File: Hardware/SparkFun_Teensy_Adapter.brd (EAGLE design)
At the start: 7 parts, among them J1 ARDUINO_R3_SHIELD, J2 AVR_SPI_PRG_6PTH

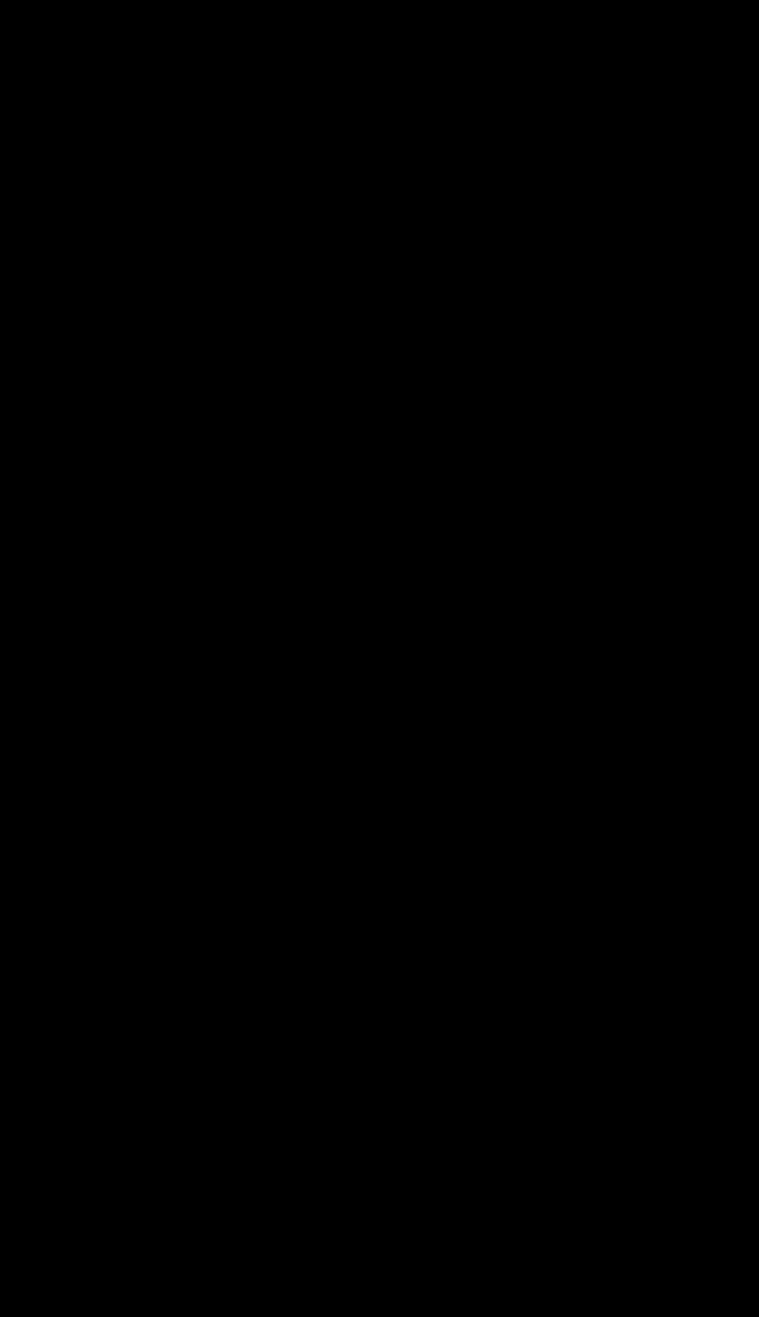
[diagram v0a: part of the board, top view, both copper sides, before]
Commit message: Basic mechanical layout of board.
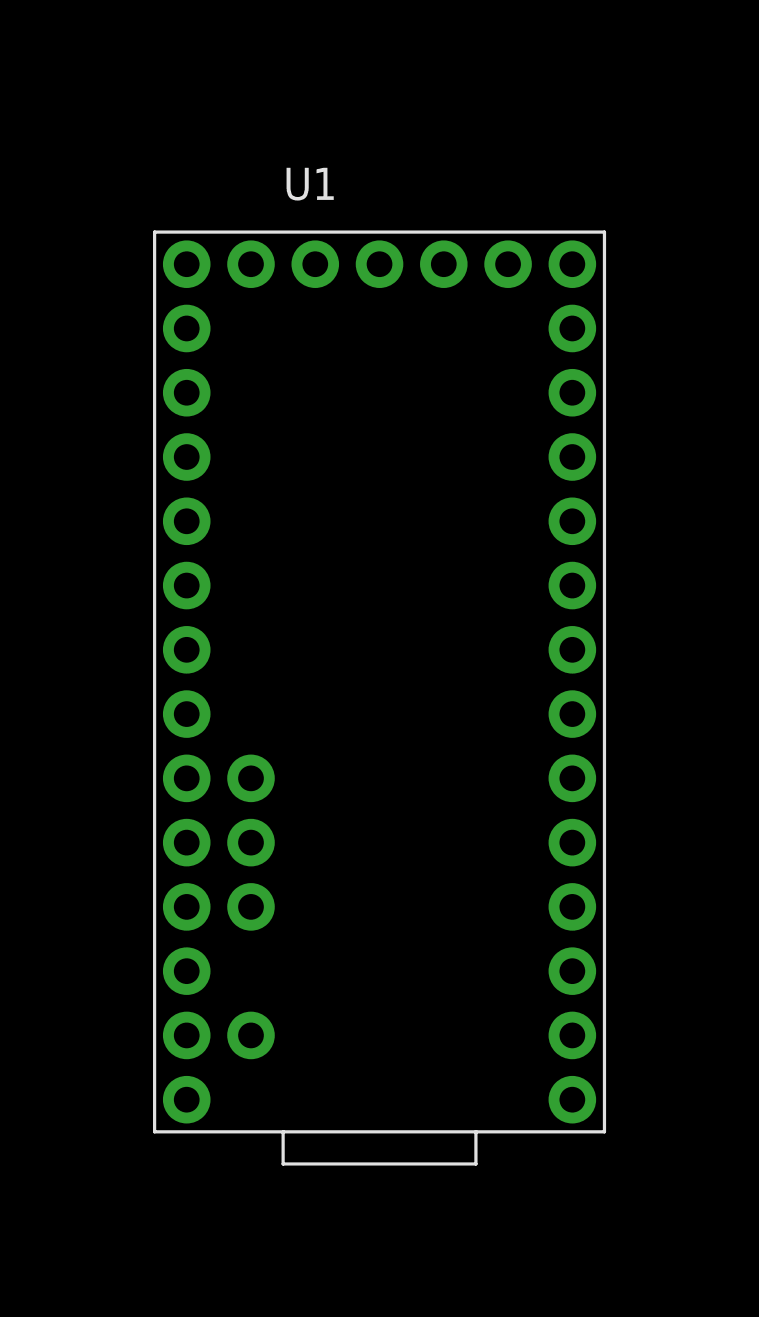
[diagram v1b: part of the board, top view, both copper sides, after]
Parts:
- added U1: TEENSY-3.1, Testing:TEENSY-3.1
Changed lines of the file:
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@@
 <layer number="251" name="SMDround" color="12" fill="11" visible="no" active="no"/>
 <layer number="254" name="cooling" color="7" fill="1" visible="no" active="yes"/>
+<layer number="255" name="routoute" color="7" fill="1" visible="yes" active="yes"/>
 </layers>
 <board>
@@
 <element name="LOGO2" library="SparkFun-Aesthetics" package="OSHW-LOGO-M" value="OSHW-LOGOM" x="29.21" y="0"/>
 <element name="J2" library="SparkFun-Connectors" package="2X3" value="AVR_SPI_PRG_6PTH" x="25.4" y="71.12"/>
+<element name="U1" library="Testing" package="TEENSY-3.1" value="TEENSY-3.1" x="20.32" y="16.51">
+<attribute name="SF_ID" value="DEV-12646" x="20.32" y="16.51" size="1.778" layer="27" font="vector" ratio="15" display="off"/>
+</element>
 </elements>
 <signals>

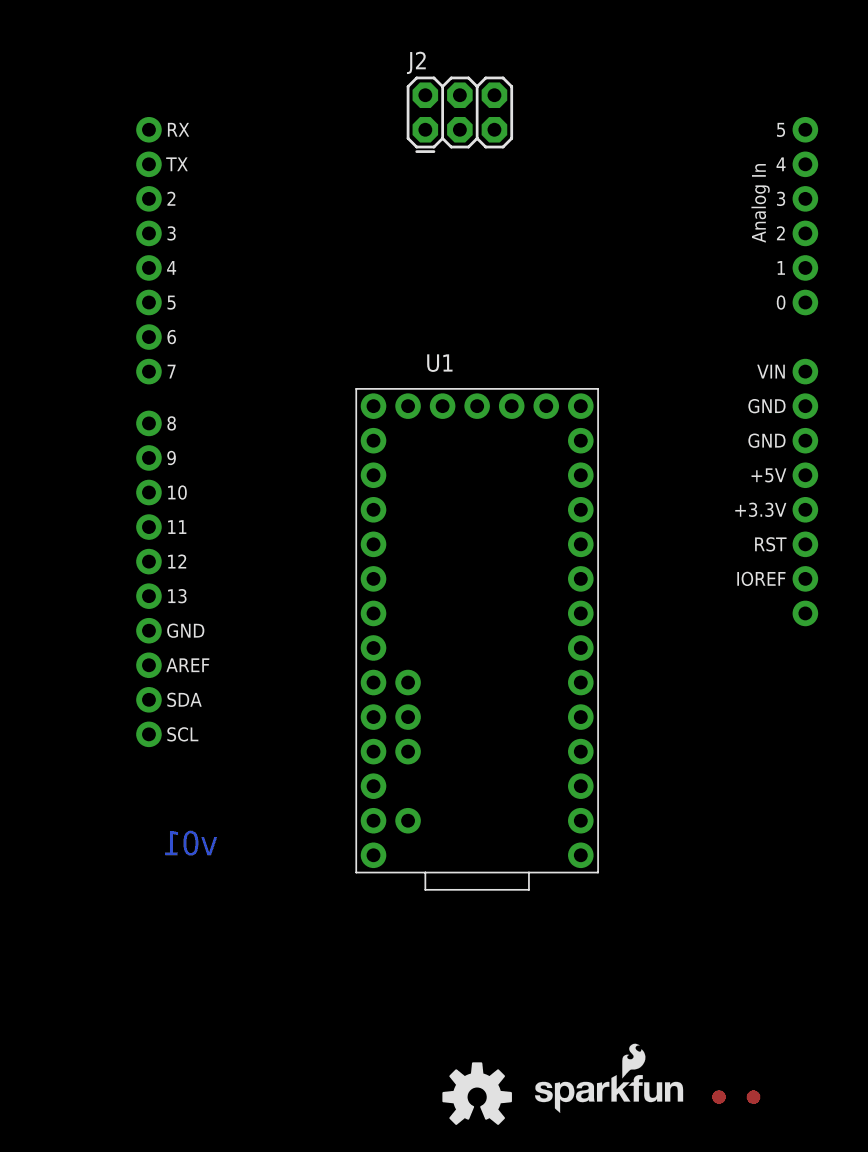
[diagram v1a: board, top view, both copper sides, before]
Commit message: Power connectors added
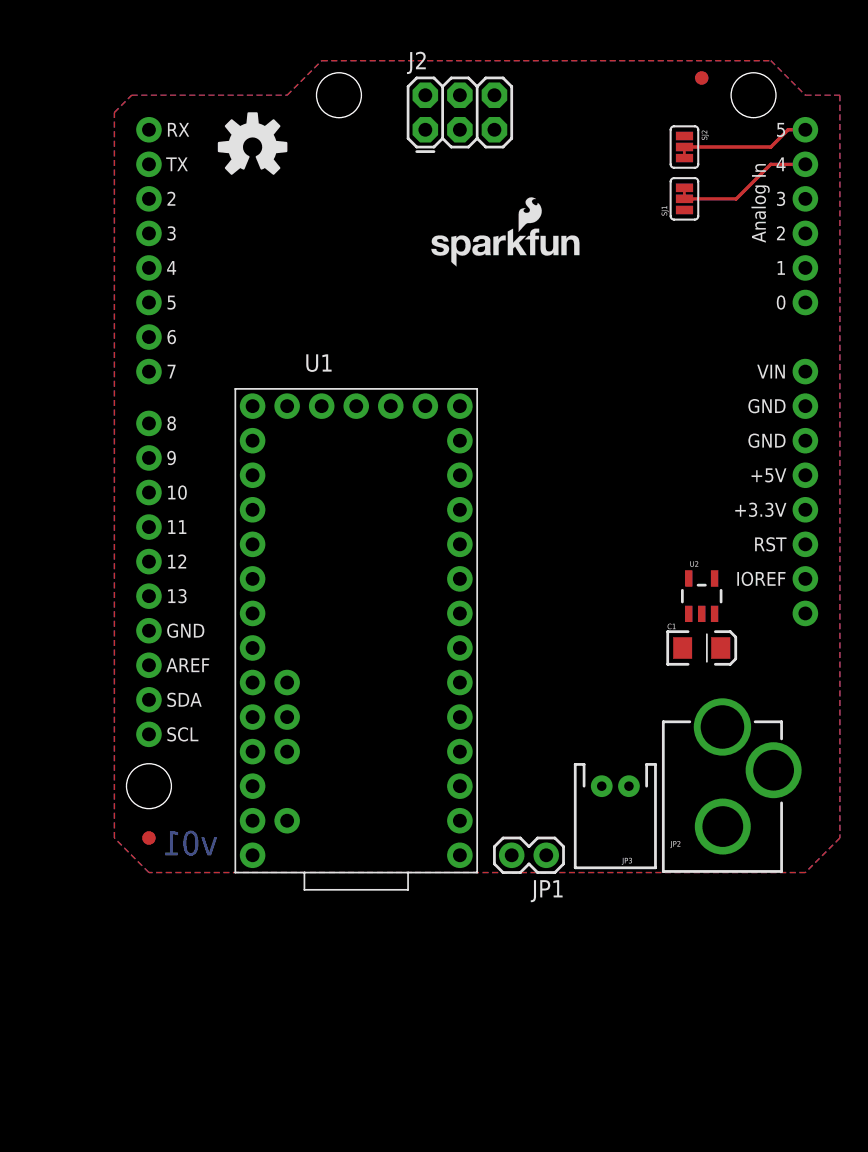
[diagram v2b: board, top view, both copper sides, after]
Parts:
- added C1: 10uF, SparkFun-Capacitors:EIA3216
- added JP1: M02PTH, SparkFun-Connectors:1X02
- added JP2: POWER_JACKPTH_LOCK, SparkFun-Connectors:POWER_JACK_PTH_LOCK
- added JP3: M02JST-PTH-2, SparkFun-Connectors:JST-2-PTH
- added SJ1, SJ2: JUMPER-PAD-3-2OF3_NC_BY_TRACE_SMALL, SparkFun-Passives:PAD-JUMPER-3-2OF3_NC_BY_TRACE_YES_SILK_FULL_BOX
- added U2: (no value), SparkFun-PowerIC:SOT23-5
- J1: value ARDUINO_R3_SHIELD -> ARDUINO_R3_SHIELDUNO_R3_SHIELD_HOLES; device SparkFun-Boards:UNO_R3_SHIELD -> Testing:UNO_R3_SHIELD_HOLES
- moved FID1 75.0 mm to (45.7, 74.9)
- moved LOGO2 71.8 mm to (12.7, 69.8)
- moved LOGO1 62.7 mm to (25.4, 61.0)
- moved FID2 46.0 mm to (5.08, 19.1)
- moved U1 8.89 mm to (11.4, 16.5)
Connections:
- new net 3.3V: J1.3.3V, J2.2, JP3.2, U1.3.3V
- new net 5V: J1.5V, U1.VIN, U2.5
- new net A0: J1.A0, U1.14
- new net A1: J1.A1, U1.15
- new net A10: U1.A10
- new net A11: U1.A11
- new net A2: J1.A2, U1.16
- new net A3: J1.A3, U1.17
- new net A4: J1.A4, SJ1.2
- new net A5: J1.A5, SJ2.2
- new net A6: SJ1.1, U1.20
- new net A7: SJ2.1
- new net A8: U1.22
- new net A9: U1.23
- new net AREF: J1.AREF, U1.AREF
- new net CS: J1.D10, U1.10
- new net D2: J1.D2, U1.2
- new net D3: J1.D3, U1.3
- new net D4: J1.D4, U1.4
- new net D5: J1.D5, U1.5
- new net D6: J1.D6, U1.6
- new net D7: J1.D7, U1.7
- new net D8: J1.D8, U1.8
- new net D9: J1.D9, U1.9
- new net GND: C1.C, J1.GND@0, J1.GND@1, J1.GND@2, J2.6, JP1.2, JP2.GND, JP2.GNDBREAK, JP3.1, U1.AGND, U1.GND, U1.GND1, U2.2
- new net MISO: J1.D12, J2.1, U1.12
- new net MOSI: J1.D11, J2.4, U1.11
- new net N$2: J1.VIN
- new net N$6: U1.VUSB
- new net PROG: U1.PROG
- new net RESET: J1.RES, J2.5
- new net RTC_BATT: JP1.1, U1.VBAT
- new net RX: J1.RX, U1.0
- new net SCK: J1.D13, J2.3, U1.13
- new net SCL: J1.SCL, SJ2.3, U1.19
- new net SDA: J1.SDA, SJ1.3, U1.18
- new net TX: J1.TX, U1.1
- new net VRAW: C1.A, JP2.PWR, U2.1, U2.3
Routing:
- net A4: track 0.00 -> 9.94 mm
- net A5: track 0.00 -> 9.42 mm
- added copper zone on layer 1, net GND
- added copper zone on layer 16, net GND

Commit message: Partial routing
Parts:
- added C2: (no value), SparkFun-Capacitors:EIA7343
- added JP4: (no value), SparkFun-Connectors:1X08_ROUND
- moved JP1 57.1 mm to (14.0, 71.1)
- moved LOGO2 7.73 mm to (14.0, 62.2)
- moved U1 6.35 mm to (17.8, 16.5)
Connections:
- removed net N$6: U1.VUSB
- new net A14/DAC: JP4.2, U1.A14/DAC
- new net HV_AREF: J1.AREF
- new net N$9: JP4.1
- new net VUSB: C2.A, JP4.7, U1.VUSB
- net A10: now also JP4.4
- net A11: now also JP4.3
- net A8: now also JP4.6
- net A9: now also JP4.5
- net AREF: no longer J1.AREF
- net GND: now also C2.C
- net PROG: now also JP4.8
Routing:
- net 3.3V: track 0.00 -> 88.3 mm, vias 0 -> 2
- net SCK: track 0.00 -> 54.3 mm
- net 5V: track 0.00 -> 53.8 mm, vias 0 -> 1
- net RESET: track 0.00 -> 42.2 mm
- net MOSI: track 0.00 -> 38.7 mm
- net D8: track 0.00 -> 34.8 mm
- net D9: track 0.00 -> 30.8 mm
- net CS: track 0.00 -> 29.7 mm, vias 0 -> 1
- net RTC_BATT: track 0.00 -> 27.7 mm
- net MISO: track 0.00 -> 24.0 mm, vias 0 -> 1
- net SDA: track 0.00 -> 20.3 mm
- net SCL: track 0.00 -> 19.1 mm
- net VRAW: track 0.00 -> 16.7 mm, vias 0 -> 1
- net A11: track 0.00 -> 11.0 mm
- net A10: track 0.00 -> 11.0 mm
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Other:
- board text added: "4-12V"

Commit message: Routing finished
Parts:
- removed C2: (no value), SparkFun-Capacitors:EIA7343
- removed JP1: M02PTH, SparkFun-Connectors:1X02
- removed JP4: (no value), SparkFun-Connectors:1X08_ROUND
- added JP6, JP7: M02PTH, SparkFun-Connectors:1X02
- added JP8: (no value), SparkFun-Connectors:1X04
- added JP9: (no value), SparkFun-Connectors:1X03
- moved C1 6.02 mm to (51.4, 31.1), turned to 180 degrees
- moved SJ2 4.02 mm to (40.6, 71.1), turned to 180 degrees
- moved SJ1 3.81 mm to (40.6, 66.0), turned to 180 degrees
- moved U2 3.70 mm to (48.9, 34.9)
- moved U1 3.18 mm to (14.6, 16.5)
- moved FID2 1.80 mm to (6.35, 17.8)
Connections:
- removed net N$9: JP4.1
- net A10: now also JP7.1; no longer JP4.4
- net A11: now also JP7.2; no longer JP4.3
- net A14/DAC: now also JP8.4; no longer JP4.2
- net A7: now also U1.21
- net A8: now also JP6.2; no longer JP4.6
- net A9: now also JP6.1; no longer JP4.5
- net AREF: now also JP9.3
- net GND: now also JP8.1, JP9.1; no longer C2.C, JP1.2
- net PROG: now also JP8.3; no longer JP4.8
- net RTC_BATT: now also JP8.2; no longer JP1.1
- net VUSB: now also JP9.2; no longer C2.A, JP4.7
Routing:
- net RX: track 0.00 -> 80.2 mm
- net TX: track 0.00 -> 78.7 mm, vias 0 -> 2
- net A7: track 0.00 -> 62.2 mm, vias 0 -> 3
- net D2: track 0.00 -> 61.5 mm, vias 0 -> 1
- net D3: track 0.00 -> 60.7 mm
- net SCL: track 19.1 -> 73.0 mm, vias 0 -> 3
- net A6: track 0.00 -> 52.5 mm, vias 0 -> 1
- net D4: track 0.00 -> 52.4 mm, vias 0 -> 1
- net A3: track 0.00 -> 51.7 mm, vias 0 -> 1
- net D5: track 0.00 -> 48.5 mm, vias 0 -> 1
- net A2: track 0.00 -> 47.9 mm, vias 0 -> 2
- net A1: track 0.00 -> 44.9 mm, vias 0 -> 1
- net SDA: track 20.3 -> 64.6 mm, vias 0 -> 3
- net D6: track 0.00 -> 43.4 mm, vias 0 -> 1
- net A0: track 0.00 -> 41.7 mm
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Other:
- board text added: "A10"
- board text added: "A11"
- board text added: "A14"
- board text added: "A6"
- board text added: "A7"
- board text added: "A8"
- board text added: "A9"
- board text added: "AREF"
- board text added: "GND"
- board text added: "PROG"
- board text added: "RTC"
- board text added: "SCL"
- board text added: "SDA"
- board text added: "VUSB"

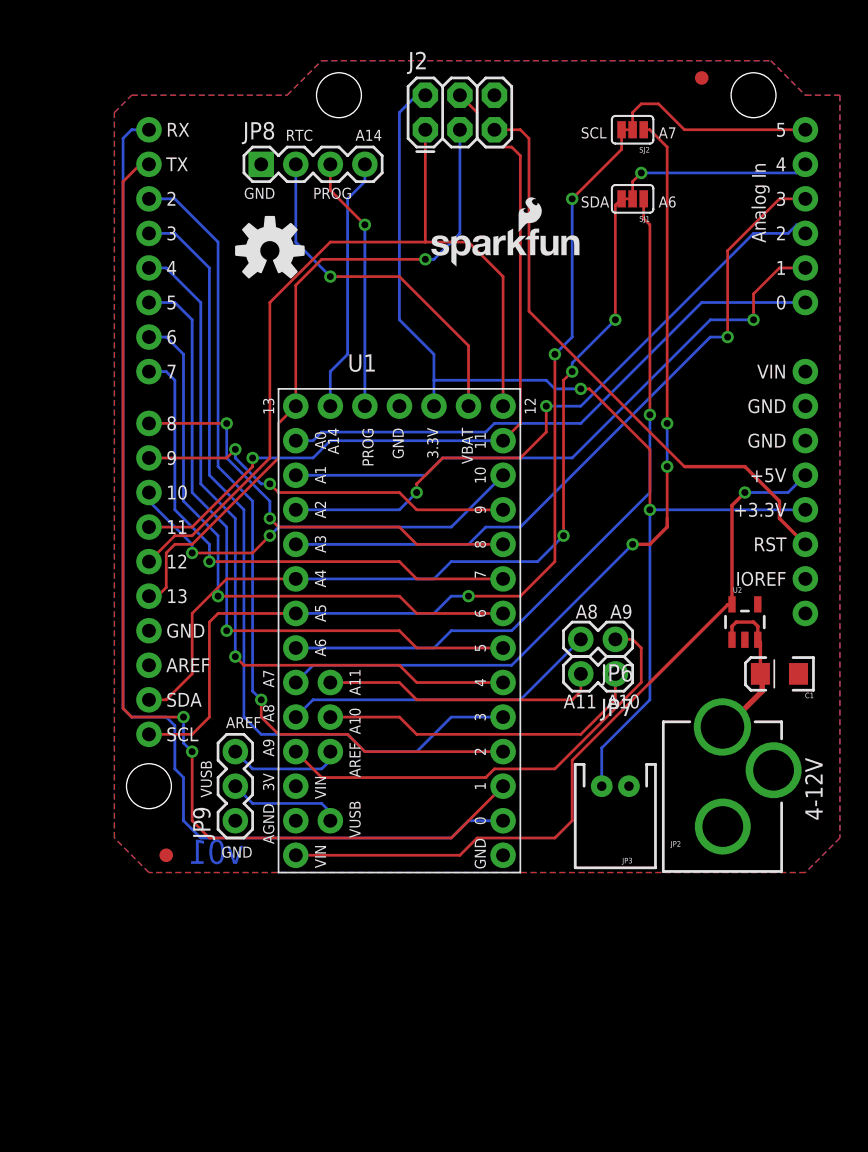
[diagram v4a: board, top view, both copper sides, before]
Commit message: Fixing DRC issues
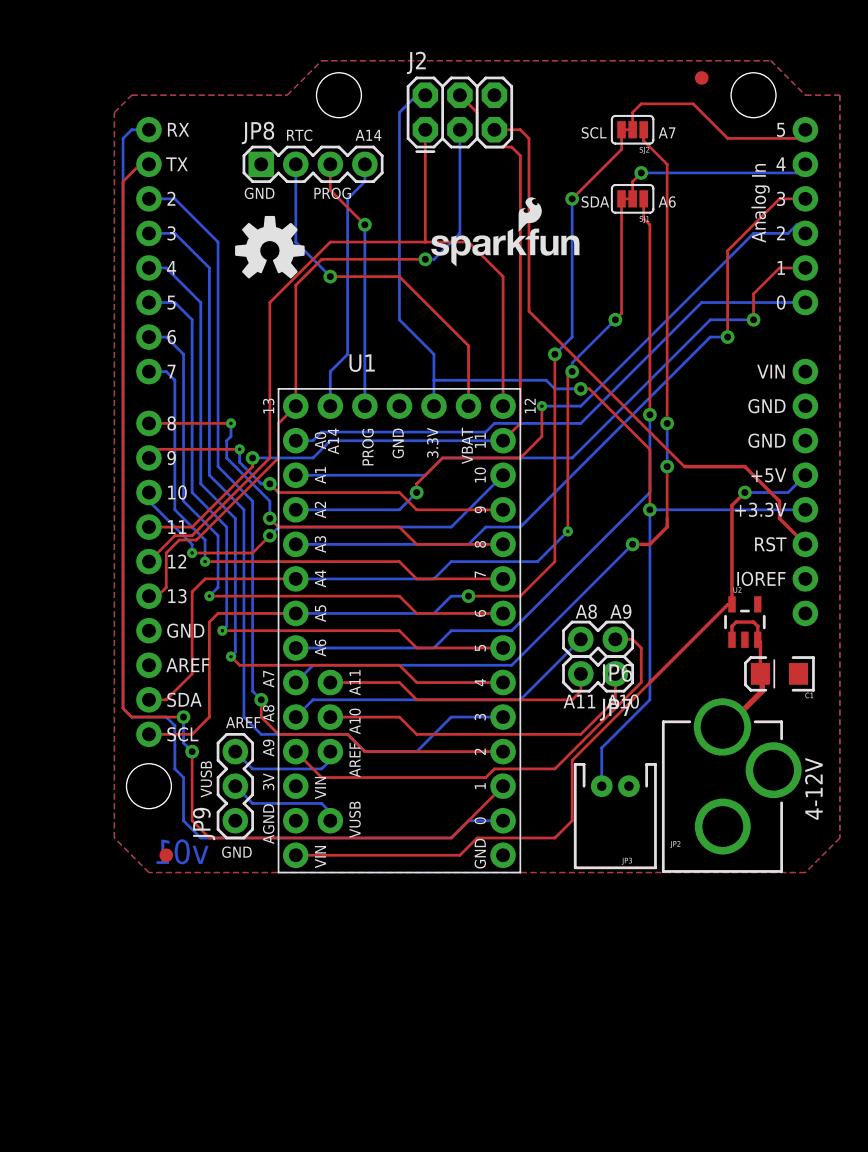
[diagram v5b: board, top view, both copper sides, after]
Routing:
- net SDA: track 64.6 -> 65.5 mm
- net D6: track 43.4 -> 44.3 mm
- net A5: track 15.0 -> 15.5 mm
